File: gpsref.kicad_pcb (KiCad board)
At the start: 4 copper layers, 77.4 x 47.8 mm, 185 parts, among them J1 SMA, J11 Debug, J12 GPS_Snoop, J13 I2C_Snoop, J2 SMA, J3 SMA, J4 SMA, J5 SMA, J6 USB_C_Receptacle_16P, Q1 AO3400A, Q2 AO3401A, T1 MABA-007159-000000, T2 MABA-007159-000000, U1 MAX-M10S, U11 74LVC1G240, U12 74LVC1G125, U13 TS5A63157DBV, U15 74LVC1G07, U2 TG5032CGN, U3 LMK05318BRGZR, U31 TMP117xxDRV, U4 STM32H503KBUx, U5 TPS82084SIL, U6 TPS82084SIL, U7 TPS7A8801RTJR, U9 TPS7A8801RTJR, Y1 32768Hz

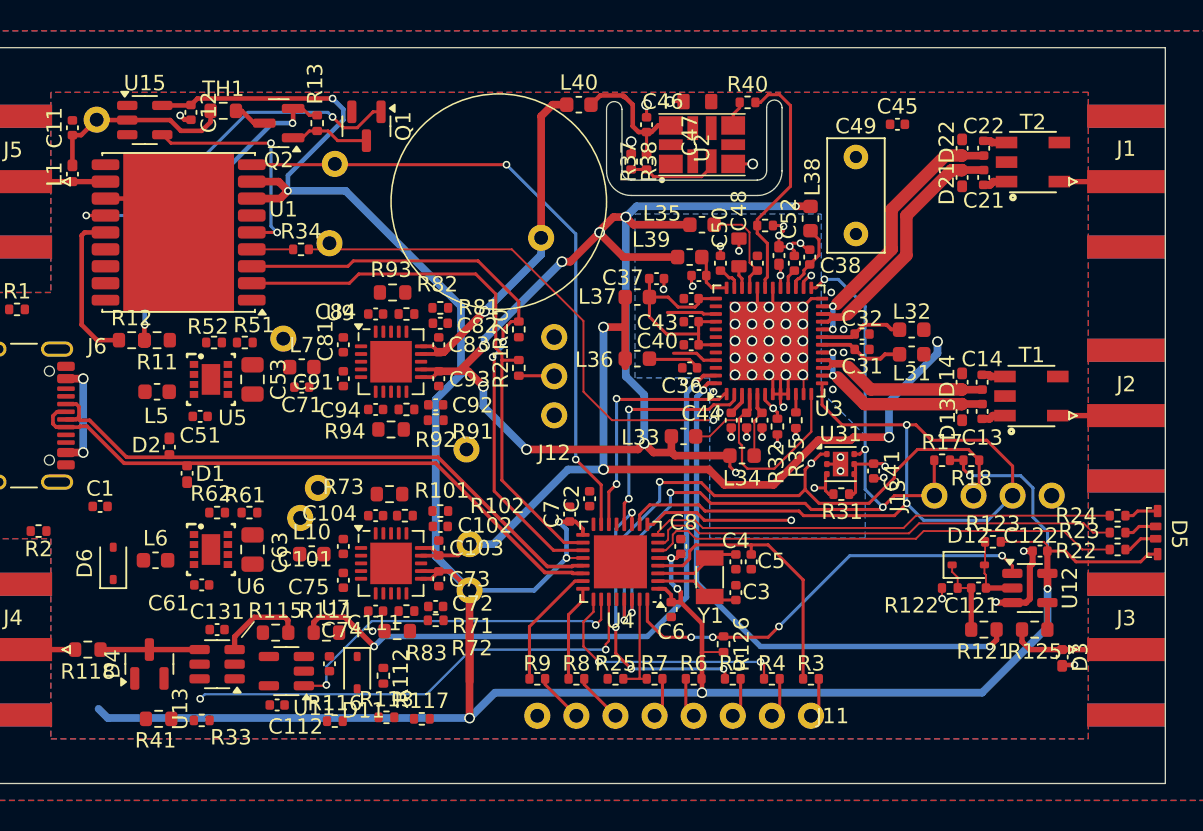
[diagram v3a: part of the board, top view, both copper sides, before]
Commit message: Supercap is back
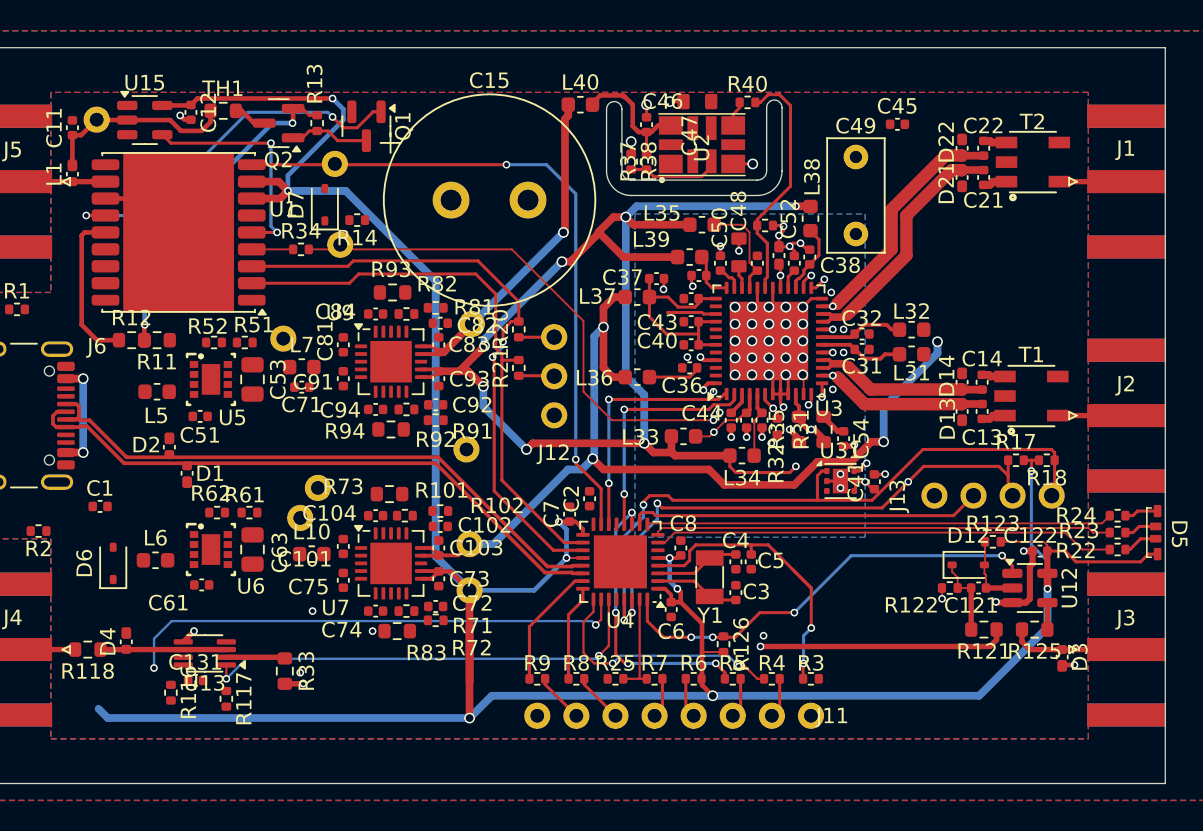
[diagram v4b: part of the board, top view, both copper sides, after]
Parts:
- removed C111, C112: 0u1, Capacitor_SMD:C_0402_1005Metric
- removed D11: 1N4148WS, Diode_SMD:D_SOD-323
- removed R111, R115: 0, Resistor_SMD:R_0603_1608Metric
- removed R112: 3k3, Resistor_SMD:R_0402_1005Metric
- removed R113: 100k, Resistor_SMD:R_0402_1005Metric
- removed R41: 66, Resistor_SMD:R_0603_1608Metric
- removed U11: 74LVC1G240, Package_TO_SOT_SMD:SOT-23-5
- added C15: .47F, Parts:CP_Radial_D13.5mm_P5.00mm, F.Cu at (131.0, 86.0)
- added C54: 0u1, Capacitor_SMD:C_0402_1005Metric, F.Cu at (156.5, 101.5)
- added D7: 1N4148WS, Diode_SMD:D_SOD-323, F.Cu at (122.8, 86.3)
- added R14: 100, Resistor_SMD:R_0402_1005Metric, F.Cu at (124.9, 87.3)
- D4: value BAS40-04 -> D_TVS; footprint Package_TO_SOT_SMD:SOT-23 -> Parts:HHS_0402
- R31: value 10k -> 200; footprint Resistor_SMD:R_0402_1005Metric -> Resistor_SMD:R_0603_1608Metric
- R33, R35: footprint Resistor_SMD:R_0402_1005Metric -> Resistor_SMD:R_0603_1608Metric
- U13: value TS5A63157DBV -> 74CB3Q3306; footprint Package_TO_SOT_SMD:SOT-23-6 -> Package_SO:VSSOP-8_2.3x2mm_P0.5mm
- moved R117 12.8 mm to (116.4, 118.4), turned to -90 degrees
- moved R116 10.8 mm to (112.8, 118.0), turned to -90 degrees
- moved TP8 7.18 mm to (132.3, 94.0)
- moved R33 6.28 mm to (120.2, 116.6), turned to -90 degrees
- moved R18 4.90 mm to (169.7, 102.9)
- moved R17 4.80 mm to (167.7, 102.9)
- moved R31 4.35 mm to (155.2, 100.9), turned to 90 degrees
- moved C131 3.58 mm to (114.4, 117.2)
- moved D4 2.08 mm to (109.9, 114.7)
- moved L36 1.20 mm to (143.1, 97.5)
- moved U31 1.10 mm to (156.3, 104.2)
- moved U13 1.06 mm to (115.0, 115.5)
- moved TP13 0.71 mm to (124.2, 89.5)
- moved C41 0.70 mm to (158.5, 104.3), turned to 90 degrees
- moved R35 0.63 mm to (153.6, 100.9)
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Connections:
- net OUT7_P renamed OUT7
- D4 pad 1: GND -> Net-(D4-A1)
- D4 pad 2: +3V3 -> GND
- J13 pad 1: I2C_SDA -> GND
- J13 pad 2: I2C_SCL -> PDN
- J13 pad 3: PDN -> I2C_SDA
- J13 pad 4: GND -> I2C_SCL
- R117 pad 2: GND -> +3V3
- R118 pad 1: Net-(D4-Pad3) -> Net-(D4-A1)
- R31 pad 1: Alert -> /Clocking/SecRefLo
- R31 pad 2: CGEN_3V3 -> /Clocking/VDD_DIG
- U1 pad 6: unconnected-(U1-V_BCKP-Pad6) -> Net-(D7-K)
- U13 pad 1: SecRef -> EN_REF2
- U13 pad 2: GND -> SecRef
- U13 pad 3: /Outputs/Ext4 -> Net-(D4-A1)
- U13 pad 4: Net-(D4-Pad3) -> GND
- U13 pad 5: +3V3 -> OUT6
- U13 pad 6: EN_REF2 -> Net-(D4-A1)
- U3 pad 45: unconnected-(U3-OUT6_P-Pad45) -> OUT6
- U3 pad 47: OUT7_N -> unconnected-(U3-OUT7_N-Pad47)
- U31 pad 3: Alert -> unconnected-(U31-ALERT-Pad3)
- U4 pad 6: /CPU/Blue -> unconnected-(U4-PA0-Pad6)
- U4 pad 7: /CPU/Green -> /CPU/Blue
- U4 pad 8: /CPU/Red -> /CPU/Green
- U4 pad 9: Alert -> /CPU/Red
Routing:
- net /Clocking/SecRefLo: track 1.19 -> 52.4 mm, vias 0 -> 2
- net OUT6: track 0.00 -> 51.1 mm, vias 0 -> 2
- net OUT7_N: track 42.8 -> 0.00 mm, vias 2 -> 0
- net I2C_SCL: track 54.5 -> 72.7 mm, vias 4 -> 3
- net I2C_SDA: track 48.7 -> 65.4 mm
- net Alert: track 16.0 -> 0.00 mm, vias 2 -> 0
- net PDN: track 49.9 -> 37.7 mm, vias 2 -> 1
- net EN_OUT4: track 23.3 -> 33.0 mm
- net Net-(D4-A1): track 0.00 -> 8.18 mm
- net Net-(D4-Pad3): track 6.44 -> 0.00 mm
- net /Outputs/Ext4: track 5.63 -> 0.00 mm
- net +3V3: track 197.0 -> 192.5 mm
- net SecRef: track 0.00 -> 3.83 mm
- net CGEN_3V3: track 94.5 -> 91.5 mm, vias 10 -> 9
- net unconnected-(U3-OUT6_P-Pad45): track 2.94 -> 0.00 mm
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
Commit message: Down to the dregs and clean-ups.
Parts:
- added C9: 1u, Capacitor_SMD:C_0402_1005Metric, F.Cu at (109.5, 97.2)
- added L11: 220, Inductor_SMD:L_0603_1608Metric, F.Cu at (112.1, 98.0)
- R51: value 180k -> 120k
- R52: value 51k -> 33k
- R61: value 82k -> 56k
- R62: value 50k -> 33k
- R71, R81, R91: value 3k6 -> 15k
- R72, R82, R92: value 1k2 -> 5k1
- R73, R83, R93: value ??? -> 82k
- R85: renamed from R102; value 1k5 -> 7k5
- R86: renamed from R101; value 1k8 -> 8k2
- R87: renamed from R94; value 10k -> 51k
- moved R83 21.9 mm to (127.1, 92.1)
- moved C45 16.9 mm to (143.2, 80.8), turned to 90 degrees
- moved R73 8.91 mm to (127.5, 114.0)
- moved R93 8.90 mm to (127.1, 100.9)
- moved R87 4.30 mm to (127.0, 105.2)
- moved TP7 2.65 mm to (134.8, 111.4)
- moved L6 1.63 mm to (112.1, 111.0)
- moved L5 1.46 mm to (112.1, 99.9)
- moved TP4 1.40 mm to (123.8, 104.7)
- moved D6 1.25 mm to (109.4, 108.4), turned to 180 degrees
- moved C1 1.03 mm to (108.6, 106.8)
- moved R2 1.03 mm to (103.3, 107.0), turned to 90 degrees
- moved TP6 1.02 mm to (120.2, 106.8)
- moved TP13 0.60 mm to (123.6, 89.2)
- moved R79 0.58 mm to (112.3, 117.7)
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- renumbered C131 to C76, C122 to C77, C121 to C78, C101 to C79, C104 to C80, C102 to C85, C103 to C86, R121 to R74, R118 to R75, R122 to R76, R123 to R77, R125 to R78, R116 to R79, R126 to R80, R117 to R84
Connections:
- net Net-(D7-K) renamed /GPS/VBCKP
- R11 pad 1: VBus -> Net-(L11-Pad2)
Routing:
- net GND: track 54.0 -> 155.6 mm, vias 63 -> 224
- net /Power/In3V3: track 0.00 -> 30.4 mm, vias 0 -> 2
- net VBus: track 7.04 -> 28.1 mm
- net /Power/2V1: track 0.00 -> 8.14 mm
- net /Power/3V6: track 0.00 -> 7.24 mm
- net /CPU/CC1: track 0.00 -> 6.62 mm
- net /GPS/VBCKP: track 0.00 -> 6.48 mm
- net /CPU/CC2: track 0.00 -> 6.45 mm
- net Net-(C15-Pad1): track 0.00 -> 6.15 mm
- net CGEN_1V8: track 60.0 -> 65.6 mm
- net /Power/In3V6: track 0.00 -> 5.52 mm
- net /Power/FbTC3: track 0.00 -> 5.45 mm
- net /Power/In2V1: track 0.00 -> 5.41 mm
- net /Power/FbCG18: track 0.00 -> 5.21 mm
- net /Power/FbCG3: track 0.00 -> 5.15 mm
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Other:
- outline, holes or cut-outs redrawn

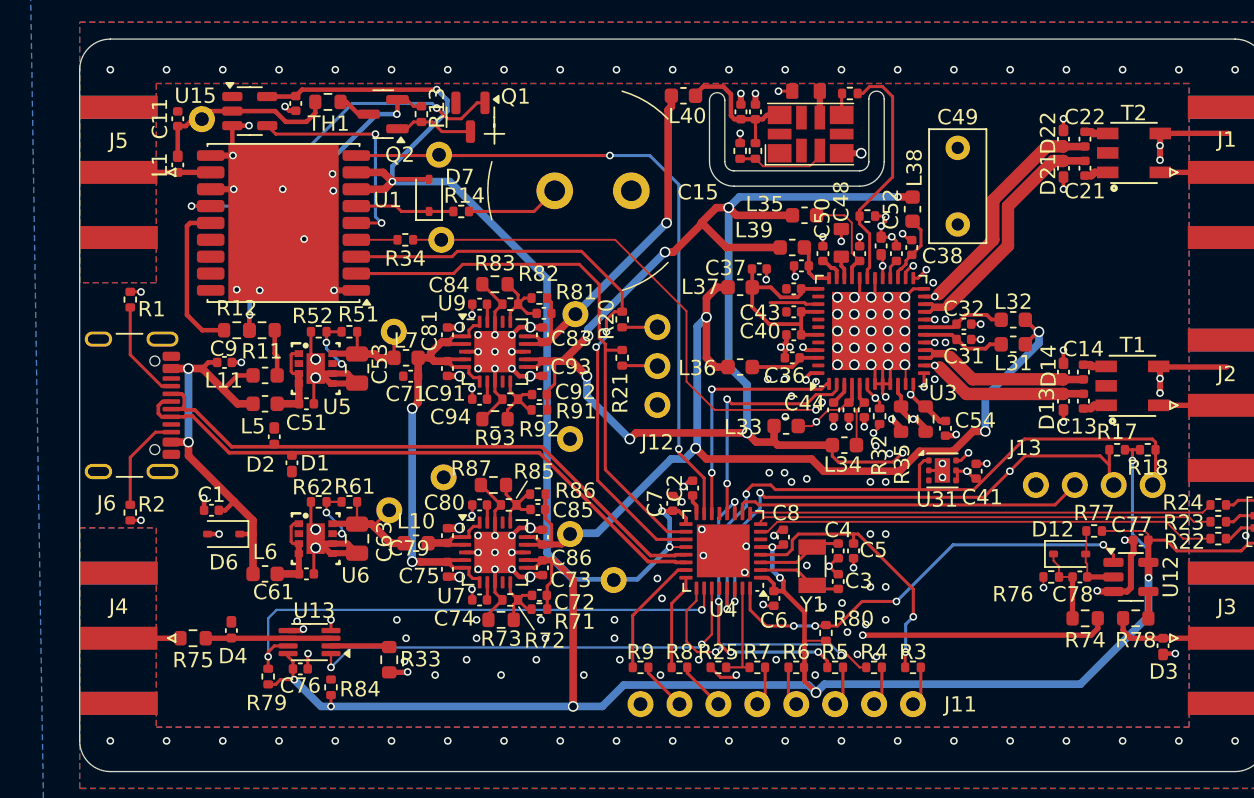
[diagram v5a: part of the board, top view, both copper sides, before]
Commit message: Add a U.Fl connector for fun.
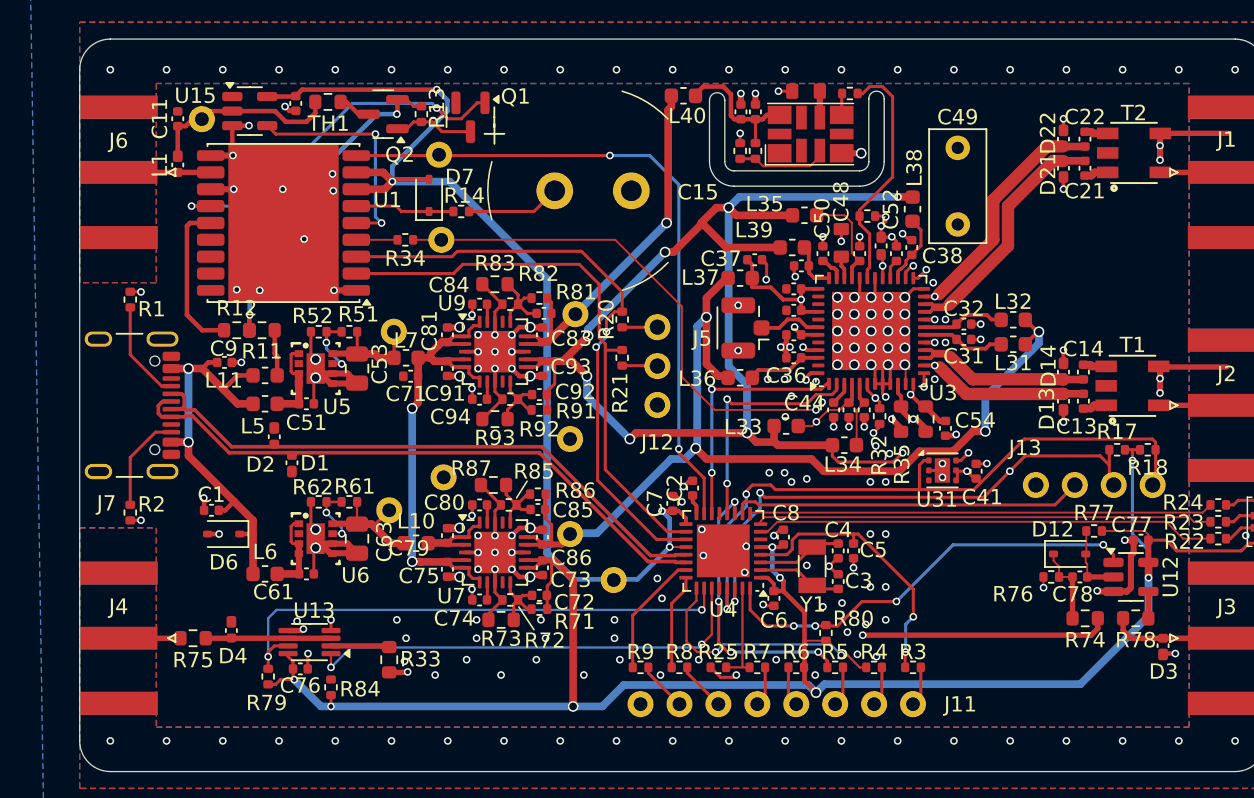
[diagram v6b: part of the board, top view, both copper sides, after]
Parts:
- added J5: U.Fl, Connector_Coaxial:U.FL_Hirose_U.FL-R-SMT-1_Vertical, F.Cu at (143.4, 95.0)
- moved L36 0.70 mm to (143.1, 98.2)
- moved C37 0.67 mm to (144.1, 90.5)
- moved L37 0.60 mm to (143.1, 91.7)
- moved C43 0.10 mm to (146.6, 93.8)
- moved C36 0.10 mm to (146.6, 96.9)
- renumbered J5 to J6, J6 to J7
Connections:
- U3 pad 42: unconnected-(U3-OUT5_P-Pad42) -> OUT5
- U4 pad 13: unconnected-(U4-PA7-Pad13) -> GND
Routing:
- net OUT5: track 0.00 -> 4.14 mm
- net unconnected-(U3-OUT4_P-Pad39): track 3.19 -> 0.00 mm
- net /Clocking/VDDO_456: track 14.9 -> 13.2 mm, vias 0 -> 2
- net /GPS/VrfSW: track 13.1 -> 12.0 mm
- net GND: track 155.6 -> 154.8 mm, vias 224 -> 226
- net /CPU/dRST: track 2.61 -> 1.89 mm
- net CGEN_1V8: track 65.6 -> 66.2 mm

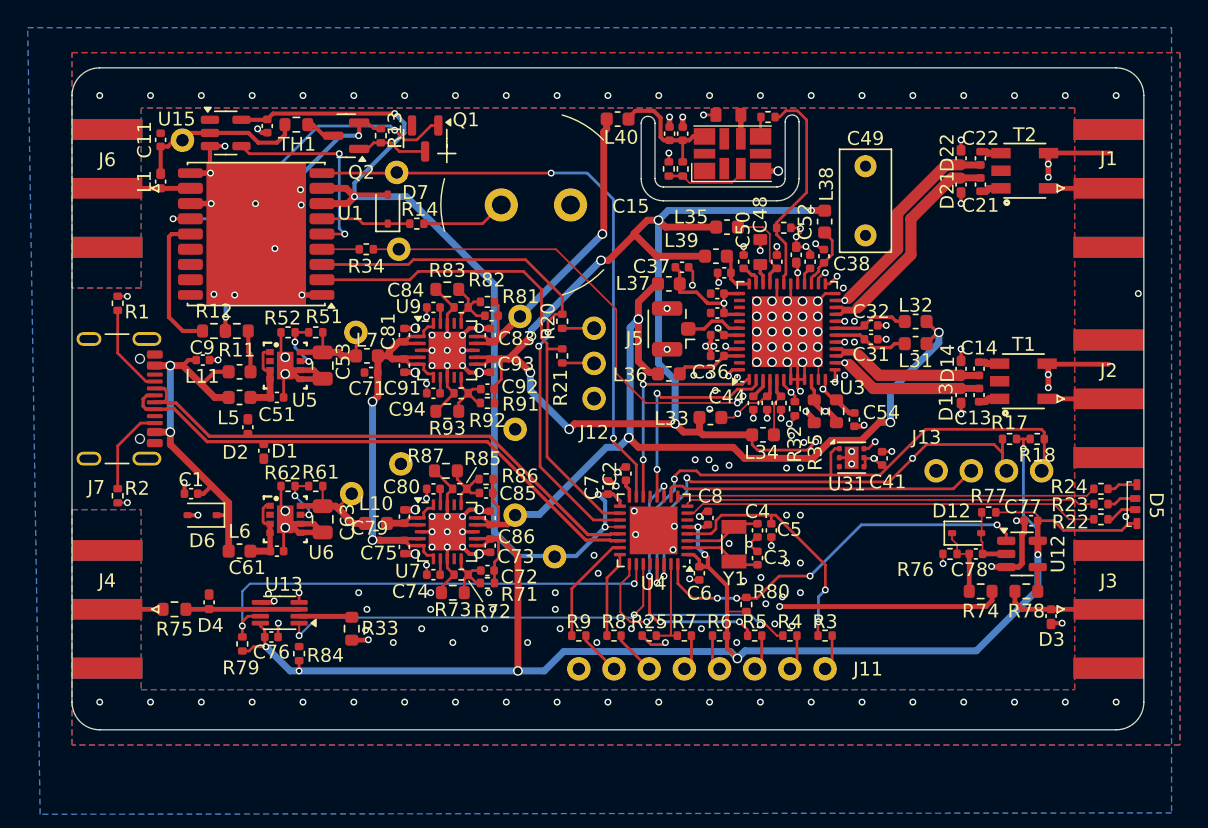
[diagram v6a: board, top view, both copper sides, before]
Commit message: DRC clean-up.  Only silk-screen noise left.
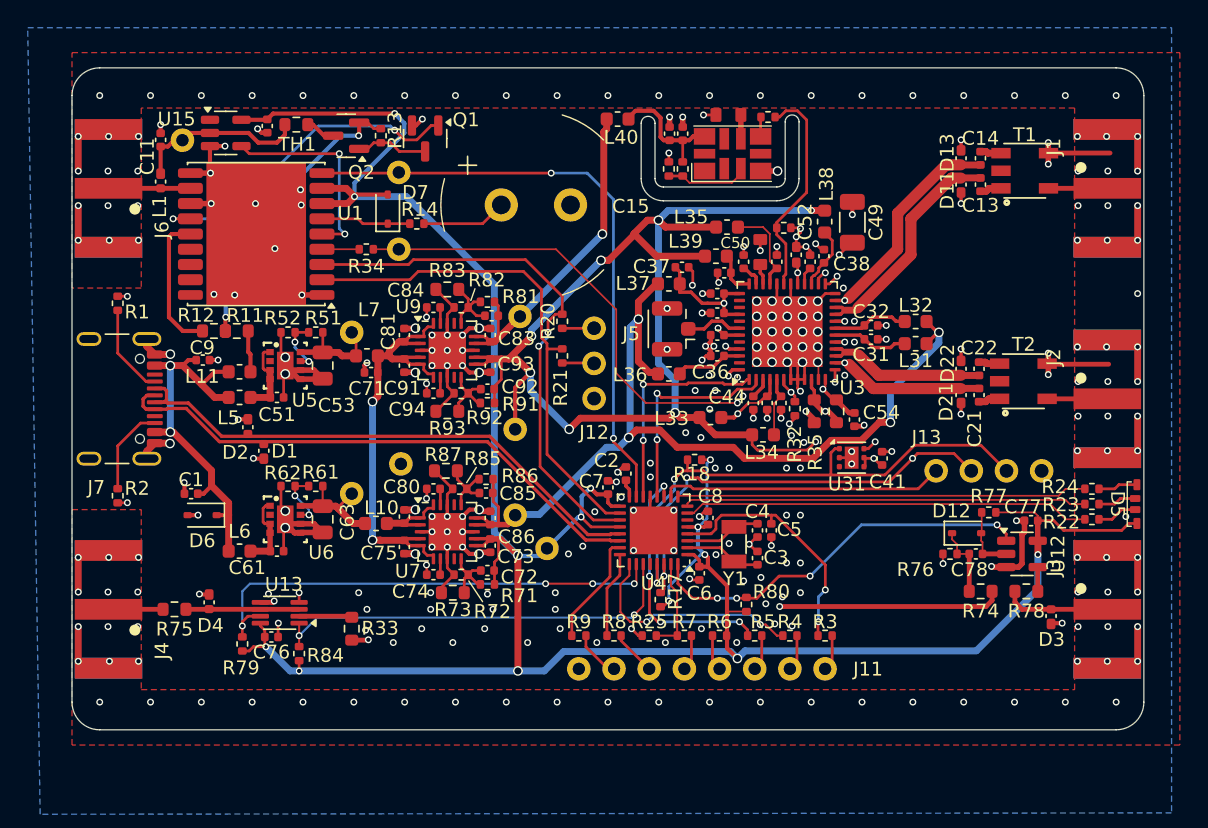
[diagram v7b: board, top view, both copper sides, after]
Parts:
- C13: renamed from C21; value 10n -> 3n3
- C14: renamed from C22; value 10n -> 3n3
- C21: renamed from C13; value 10n -> 3n3
- C22: renamed from C14; value 10n -> 3n3
- C49: footprint Capacitor_THT:C_Rect_L7.2mm_W3.5mm_P5.00mm_FKS2_FKP2_MKS2_MKP2 -> Capacitor_SMD:C_1206_3216Metric
- J1, J2, J3, J4, J6: footprint Connector_Coaxial:SMA_Amphenol_132289_EdgeMount -> Parts:SMA_Amphenol_132289_EdgeMount
- J5: footprint Connector_Coaxial:U.FL_Hirose_U.FL-R-SMT-1_Vertical -> Parts:U.FL_Hirose_U.FL-R-SMT-1_Vertical
- R51: value 120k -> 200k
- R52: value 33k -> 56k
- R61: value 56k -> 39k
- R62: value 33k -> 24k
- moved R17 27.7 mm to (142.5, 114.5), turned to -90 degrees
- moved R18 24.8 mm to (145.0, 104.4), turned to 0 degrees
- moved C49 1.34 mm to (156.3, 87.2)
- moved TP7 0.81 mm to (134.3, 110.8)
- moved R22 0.65 mm to (173.7, 108.7)
- moved R23 0.65 mm to (173.7, 107.6)
- moved R24 0.65 mm to (173.7, 106.5)
- moved TP5 0.30 mm to (120.2, 95.2)
- moved TP12 0.15 mm to (123.6, 83.7)
- moved R71 0.10 mm to (130.0, 113.4)
- renumbered D21 to D11, D22 to D13, D13 to D21, D14 to D22, T2 to T1, T1 to T2
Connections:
- net OUT6 renamed OUT4
- net OUT7 renamed OUT3
- C13 pad 1: OUT2_P -> OUT1_P
- C13 pad 2: /Outputs/AC2_P -> /Outputs/AC1_P
- C14 pad 1: OUT2_N -> OUT1_N
- C14 pad 2: /Outputs/AC2_N -> /Outputs/AC1_N
- C21 pad 1: OUT0_P -> OUT2_P
- C21 pad 2: /Outputs/AC0_P -> /Outputs/AC2_P
- C22 pad 1: OUT0_N -> OUT2_N
- C22 pad 2: /Outputs/AC0_N -> /Outputs/AC2_N
- D11 pad 1: OUT2_P -> OUT1_P
- D13 pad 1: OUT2_N -> OUT1_N
- D21 pad 1: OUT0_P -> OUT2_P
- D22 pad 1: OUT0_N -> OUT2_N
- J1 pad 1: /Outputs/Ext2 -> /Outputs/Ext1
- J13 pad 1: GND -> PDN
- J13 pad 2: PDN -> I2C_SDA
- J13 pad 3: I2C_SDA -> I2C_SCL
- J13 pad 4: I2C_SCL -> GND
- J2 pad 1: /Outputs/Ext1 -> /Outputs/Ext2
- T1 pad 1: /Outputs/AC2_P -> /Outputs/AC1_P
- T1 pad 3: /Outputs/AC2_N -> /Outputs/AC1_N
- T1 pad 5: /Outputs/Ext2 -> /Outputs/Ext1
- T2 pad 1: /Outputs/AC0_P -> /Outputs/AC2_P
- T2 pad 3: /Outputs/AC0_N -> /Outputs/AC2_N
- T2 pad 5: /Outputs/Ext1 -> /Outputs/Ext2
- U3 pad 14: OUT0_P -> OUT2_P
- U3 pad 15: OUT0_N -> OUT2_N
- U3 pad 16: OUT0_N -> OUT2_N
- U3 pad 17: OUT0_P -> OUT2_P
- U3 pad 20: OUT2_N -> OUT1_N
- U3 pad 21: OUT2_P -> OUT1_P
- U3 pad 22: OUT2_P -> OUT1_P
- U3 pad 23: OUT2_N -> OUT1_N
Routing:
- net GND: track 154.8 -> 189.9 mm, vias 226 -> 303
- net OUT1_N: track 0.00 -> 17.9 mm, vias 0 -> 2
- net OUT1_P: track 0.00 -> 16.9 mm
- net OUT0_P: track 13.0 -> 0.00 mm, vias 2 -> 0
- net OUT0_N: track 12.0 -> 0.00 mm
- net I2C_SCL: track 72.4 -> 63.1 mm
- net I2C_SDA: track 64.4 -> 58.1 mm
- net OUT2_N: track 17.9 -> 12.0 mm, vias 2 -> 0
- net PDN: track 36.4 -> 31.3 mm
- net OUT2_P: track 16.9 -> 13.0 mm, vias 0 -> 2
- net CGEN_3V3: track 94.7 -> 98.0 mm
- net +3V3: track 194.6 -> 197.2 mm, vias 12 -> 14
- net /Outputs/AC1_P: track 0.00 -> 1.57 mm
- net /Outputs/AC0_P: track 1.57 -> 0.00 mm
- net /Outputs/AC1_N: track 0.00 -> 1.53 mm
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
